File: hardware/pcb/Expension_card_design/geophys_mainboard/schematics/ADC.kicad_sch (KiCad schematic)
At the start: 52 parts, among them U12 AD7779ACPZ, Y1 OT2JI-111-8.192M

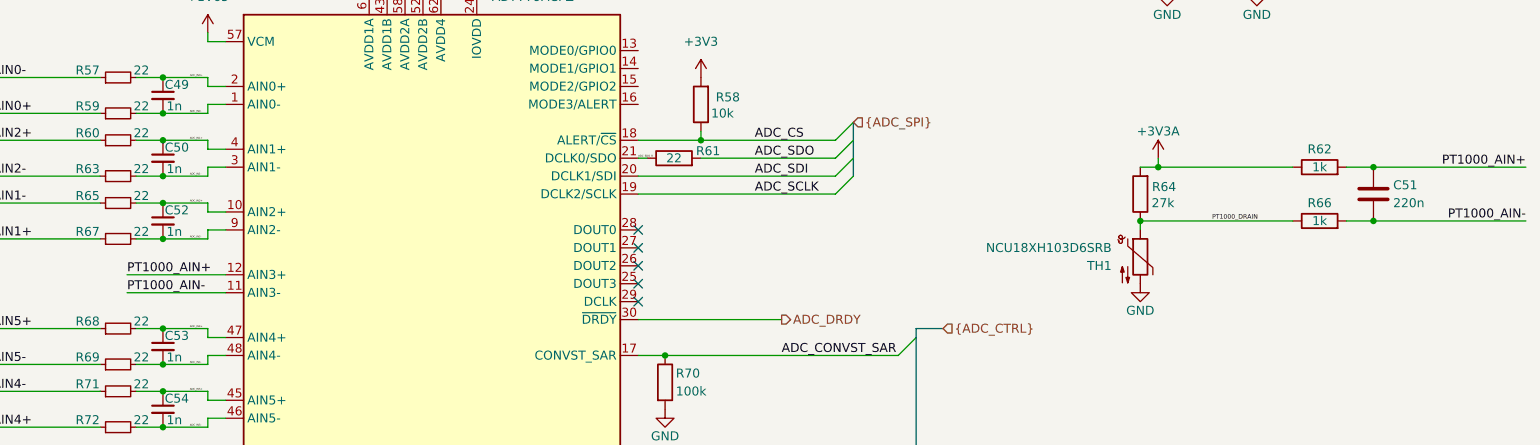
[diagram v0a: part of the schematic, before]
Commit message: Somewhat fix the ad7779 driver to read the thermistor but error with divider
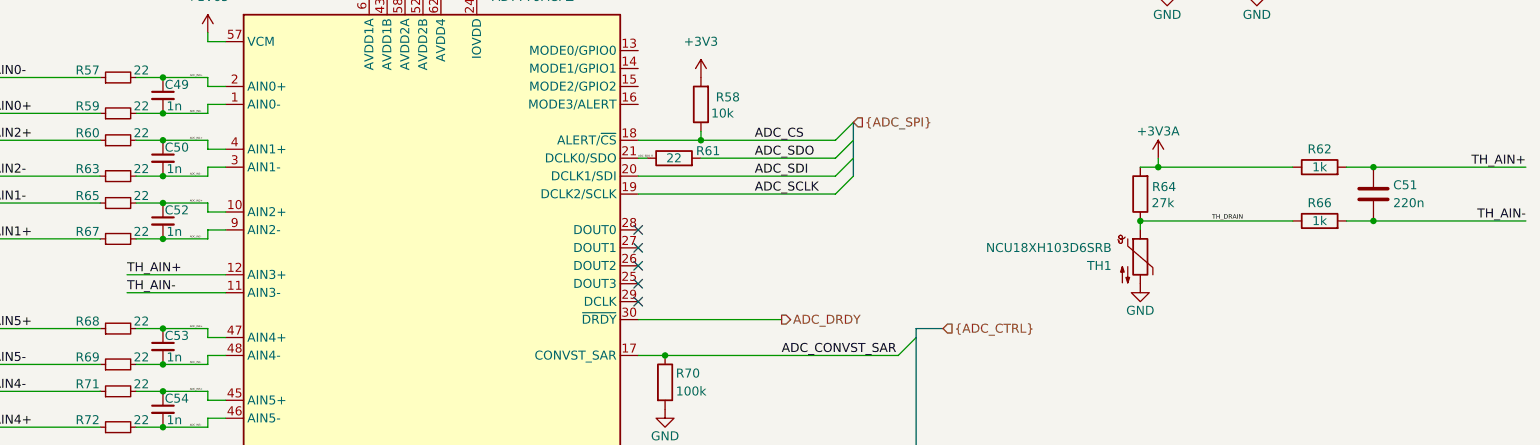
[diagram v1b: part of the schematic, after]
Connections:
- net PT1000_AIN+ renamed TH_AIN+
- net PT1000_AIN- renamed TH_AIN-
- net PT1000_DRAIN renamed TH_DRAIN

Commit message: Bring up thermistor logging with IMU temperature references
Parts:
- R64: value 27k -> 2k4
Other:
- note added: "ERREUR de composant"
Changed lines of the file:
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@@
 		)
 	)
+	(text "ERREUR de composant"
+		(exclude_from_sim no)
+		(at 201.422 72.898 0)
+		(effects
+			(font
+				(size 1.27 1.27)
+			)
+		)
+	)
 	(junction
 		(at 247.65 68.58)
@@
 			)
 		)
-		(property "Value" "27k"
+		(property "Value" "2k4"
 			(at 219.456 73.66 0)
 			(effects

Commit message: Backup avant deletion offset/dac
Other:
- note removed: "ERREUR de composant"
